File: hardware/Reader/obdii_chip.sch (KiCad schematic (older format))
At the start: 23 parts

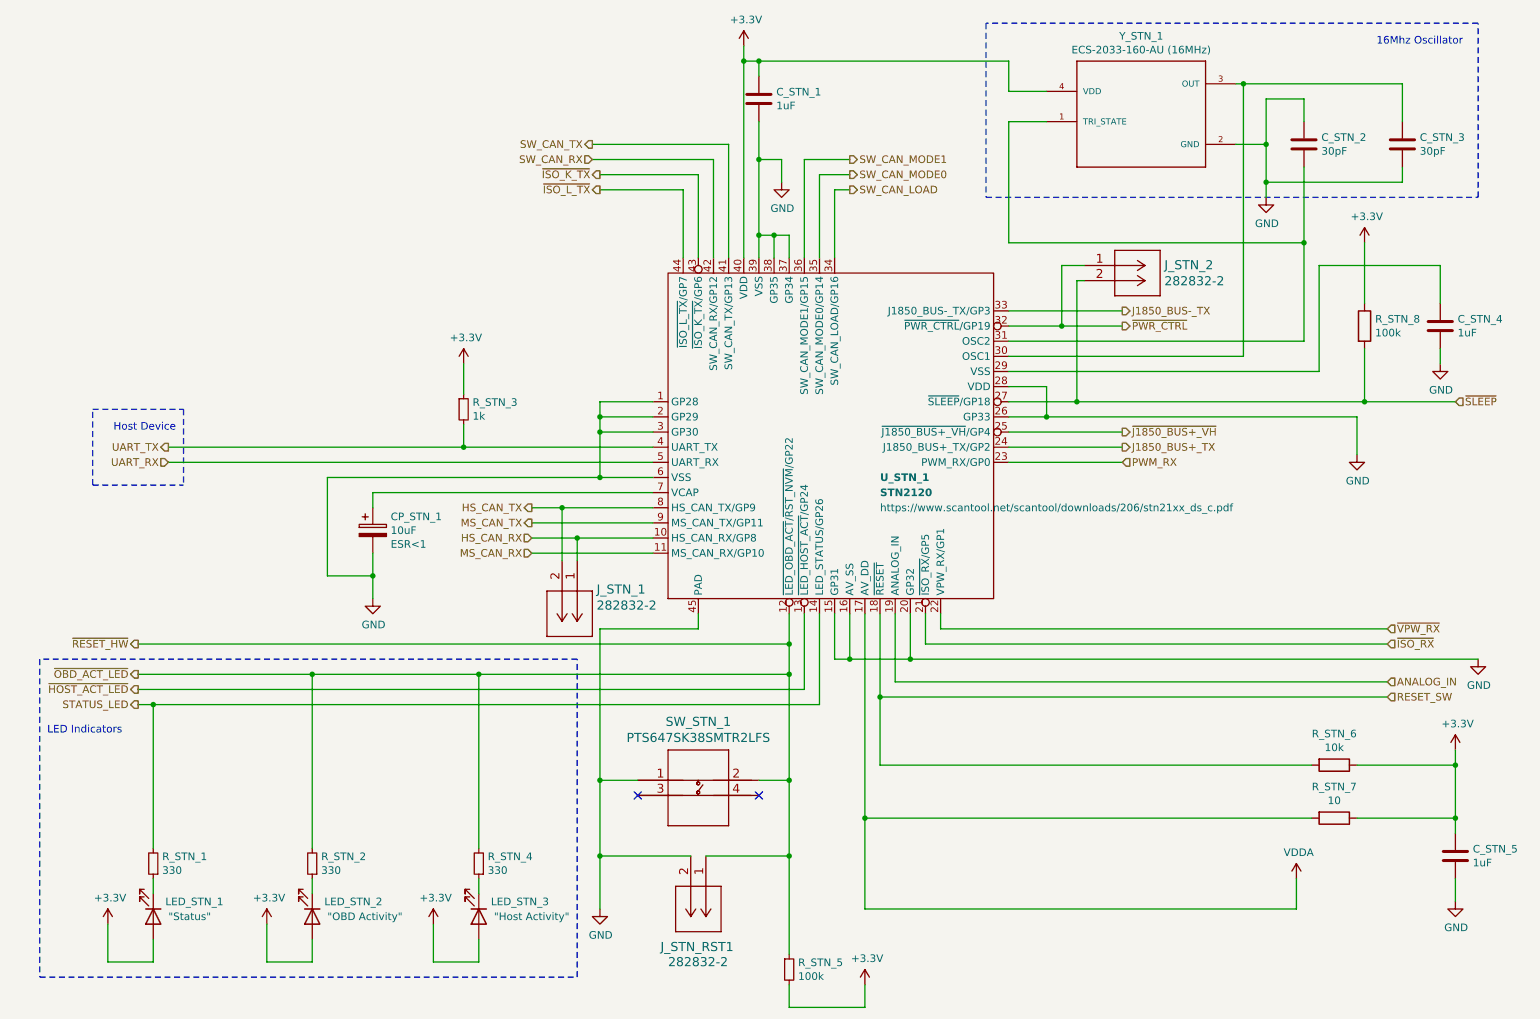
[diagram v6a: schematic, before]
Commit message: Fixed bugs in schematic. Updated BOM list. Swapped to using ESP32 holder. Updated PCB layout to v0.0.2. Updated schematic to v0.0.4
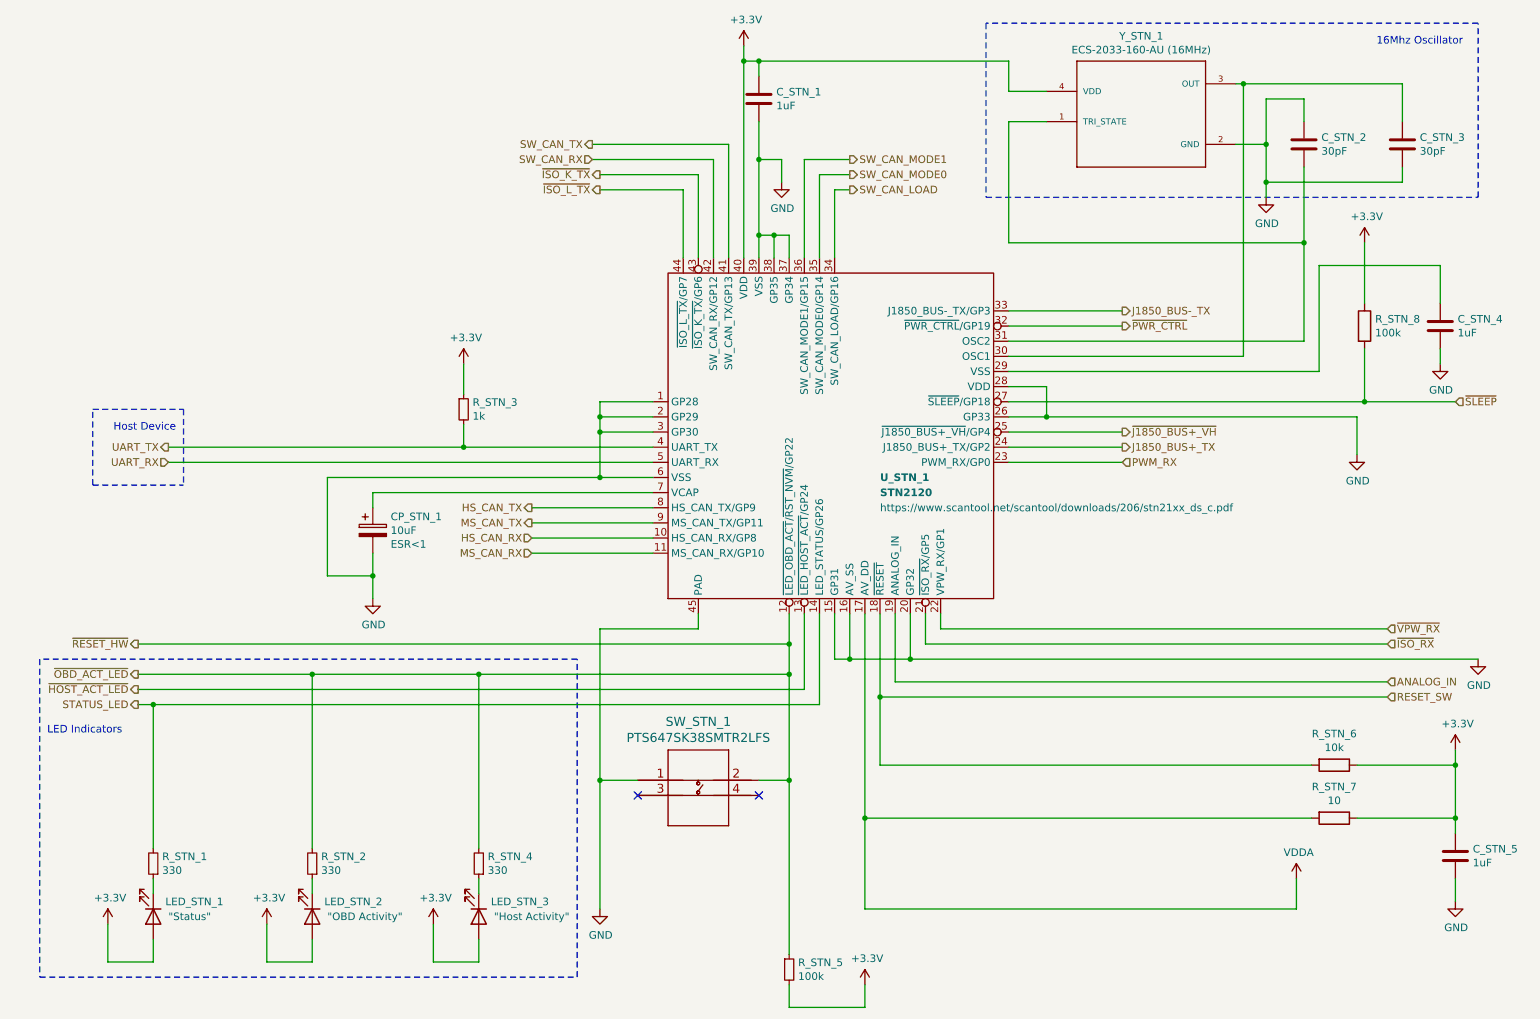
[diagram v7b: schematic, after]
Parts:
- removed J_STN_1, J_STN_2, J_STN_RST1: 282832-2, footprints:282832-2, symbol 2828322:282832-2
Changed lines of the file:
@@
 Sheet 10 19
 Title "CANnect Reader | OBDII Chip (STN2110)"
-Date "2020-10-27"
-Rev "0.0.03"
+Date "2020-10-28"
+Rev "0.0.04"
 Comp "CANtech"
 Comment1 "Created by Choong Jin Ng | jin8383@gmail.com"
@@
 	7100 1350 7100 2150
 Wire Wire Line
-	7100 3200 7550 3200
-Wire Wire Line
 	9450 2550 9450 2150
 Wire Wire Line
@@
 Wire Wire Line
 	9150 2300 9950 2300
-$Comp
-L 2828322:282832-2 J_STN_1
-U 1 1 5F9472A1
-P 4250 4250
-F 0 "J_STN_1" V 4439 4378 60  0000 L CNN
-F 1 "282832-2" V 4545 4378 60  0000 L CNN
-F 2 "footprints:282832-2" H 4650 4190 60  0001 C CNN
-F 3 "https://www.te.com/commerce/DocumentDelivery/DDEController?Action=srchrtrv&DocNm=282832&DocType=Customer+Drawing&DocLang=English" H 4250 4250 60  0001 C CNN
-F 4 "282832-2" H 4250 4250 50  0001 C CNN "Part Name"
-F 5 "DigiKey Canada" H 4250 4250 50  0001 C CNN "Vendor"
-F 6 "TE Connectivity AMP Connectors" H 4250 4250 50  0001 C CNN "Manufacturer"
-F 7 "A113314-ND" H 4250 4250 50  0001 C CNN "digikeypn"
-	1    4250 4250
-	0    1    1    0
-$EndComp
-Wire Wire Line
-	3950 3900 4150 3900
 Wire Wire Line
 	3950 4000 4750 4000
 Wire Wire Line
-	3950 4100 4250 4100
-Wire Wire Line
 	3950 4200 4750 4200
 Wire Wire Line
-	4150 4250 4150 3900
-Connection ~ 4150 3900
-Wire Wire Line
-	4150 3900 4750 3900
-Wire Wire Line
-	4250 4250 4250 4100
-Connection ~ 4250 4100
-Wire Wire Line
-	4250 4100 4750 4100
-$Comp
-L 2828322:282832-2 J_STN_2
-U 1 1 5F9BC402
-P 7600 2300
-F 0 "J_STN_2" H 8128 2303 60  0000 L CNN
-F 1 "282832-2" H 8128 2197 60  0000 L CNN
-F 2 "footprints:282832-2" H 8000 2240 60  0001 C CNN
-F 3 "https://www.te.com/commerce/DocumentDelivery/DDEController?Action=srchrtrv&DocNm=282832&DocType=Customer+Drawing&DocLang=English" H 7600 2300 60  0001 C CNN
-F 4 "282832-2" H 7600 2300 50  0001 C CNN "Part Name"
-F 5 "DigiKey Canada" H 7600 2300 50  0001 C CNN "Vendor"
-F 6 "TE Connectivity AMP Connectors" H 7600 2300 50  0001 C CNN "Manufacturer"
-F 7 "A113314-ND" H 7600 2300 50  0001 C CNN "digikeypn"
-	1    7600 2300
-	1    0    0    -1
-$EndComp
-Wire Wire Line
-	7100 2700 7450 2700
-Wire Wire Line
-	7600 2300 7450 2300
-Wire Wire Line
-	7450 2300 7450 2700
-Connection ~ 7450 2700
-Wire Wire Line
-	7450 2700 7850 2700
-Wire Wire Line
-	7600 2400 7550 2400
-Wire Wire Line
-	7550 2400 7550 3200
-Connection ~ 7550 3200
-Wire Wire Line
-	7550 3200 9450 3200
-Wire Wire Line
 	5650 7200 5650 7050
-$Comp
-L 2828322:282832-2 J_STN_RST1
-U 1 1 5FA37F1D
-P 5100 6200
-F 0 "J_STN_RST1" V 5700 5900 60  0000 L CNN
-F 1 "282832-2" V 5800 5950 60  0000 L CNN
-F 2 "footprints:282832-2" H 5500 6140 60  0001 C CNN
-F 3 "https://www.te.com/commerce/DocumentDelivery/DDEController?Action=srchrtrv&DocNm=282832&DocType=Customer+Drawing&DocLang=English" H 5100 6200 60  0001 C CNN
-F 4 "282832-2" H 5100 6200 50  0001 C CNN "Part Name"
-F 5 "DigiKey Canada" H 5100 6200 50  0001 C CNN "Vendor"
-F 6 "TE Connectivity AMP Connectors" H 5100 6200 50  0001 C CNN "Manufacturer"
-F 7 "A113314-ND" H 5100 6200 50  0001 C CNN "digikeypn"
-	1    5100 6200
-	0    1    1    0
-$EndComp
 Connection ~ 6250 5150
 Wire Wire Line
@@
 Connection ~ 5650 5700
 Wire Wire Line
-	5650 5700 5650 6200
-Wire Wire Line
 	4650 5700 4400 5700
 Connection ~ 4400 5700
 Wire Wire Line
-	4400 5700 4400 6200
-Wire Wire Line
 	5650 7200 6150 7200
 Wire Wire Line
 	6150 7200 6150 7050
-Wire Wire Line
-	5100 6200 5650 6200
-Connection ~ 5650 6200
-Wire Wire Line
-	5650 6200 5650 6850
-Wire Wire Line
-	5000 6200 4400 6200
-Connection ~ 4400 6200
-Wire Wire Line
-	4400 6200 4400 6550
 $Comp
 L PTS647SK38SMTR2LFS:PTS647SK38SMTR2LFS SW_STN_1
@@
 NoConn ~ 4650 5800
 NoConn ~ 5450 5800
+Wire Wire Line
+	3950 3900 4750 3900
+Wire Wire Line
+	3950 4100 4750 4100
+Wire Wire Line
+	7100 2700 7850 2700
+Wire Wire Line
+	7100 3200 9450 3200
+Wire Wire Line
+	5650 5700 5650 6850
+Wire Wire Line
+	4400 5700 4400 6550
 $EndSCHEMATC

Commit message: Revising reader
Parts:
- removed SW_STN_1: PTS647SK38SMTR2LFS, footprints:PTS647SK38SMTR2LFS, symbol PTS647SK38SMTR2LFS:PTS647SK38SMTR2LFS
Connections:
- net ~HOST_ACT_LED~: now also R_STN_4.2
- net ~OBD_ACT_LED~: no longer R_STN_4.2
- no-connect marks 2 -> 0
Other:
- note added: "Insert jumper here"
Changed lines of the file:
@@
 Sheet 10 19
 Title "CANnect Reader | OBDII Chip (STN2110)"
-Date "2020-10-28"
-Rev "0.0.04"
+Date "2020-11-19"
+Rev "0.0.05"
 Comp "CANtech"
 Comment1 "Created by Choong Jin Ng | jin8383@gmail.com"
@@
 U 1 1 5FC10F0A
 P 5650 6950
-F 0 "R_STN_5" H 5709 6996 50  0000 L CNN
-F 1 "100k" H 5709 6905 50  0000 L CNN
+F 0 "R_STN_5" H 5250 7000 50  0000 L CNN
+F 1 "100k" H 5350 6900 50  0000 L CNN
 F 2 "footprints:RESC1608X55N" H 5650 6950 50  0001 C CNN
 F 3 "https://www.yageo.com/upload/media/product/productsearch/datasheet/rchip/PYu-RT_1-to-0.01_RoHS_L_12.pdf" H 5650 6950 50  0001 C CNN
@@
 L power:+3.3V #PWR064
 U 1 1 5FC11757
-P 6150 7050
-F 0 "#PWR064" H 6150 6900 50  0001 C CNN
-F 1 "+3.3V" H 6165 7223 50  0000 C CNN
-F 2 "" H 6150 7050 50  0001 C CNN
-F 3 "" H 6150 7050 50  0001 C CNN
-	1    6150 7050
+P 5900 7050
+F 0 "#PWR064" H 5900 6900 50  0001 C CNN
+F 1 "+3.3V" H 5915 7223 50  0000 C CNN
+F 2 "" H 5900 7050 50  0001 C CNN
+F 3 "" H 5900 7050 50  0001 C CNN
+	1    5900 7050
 	1    0    0    -1
 $EndComp
@@
 	2500 5000 2500 6150
 Wire Wire Line
-	3600 5000 3600 6150
-Wire Wire Line
 	3600 6900 3300 6900
 Wire Wire Line
@@
 	1350 4800 5650 4800
 Wire Wire Line
-	1350 5100 5750 5100
+	1350 5100 3600 5100
 Wire Wire Line
 	1350 5200 1450 5200
@@
 Wire Wire Line
 	2500 5000 1350 5000
-Connection ~ 3600 5000
-Wire Wire Line
-	2500 5000 3600 5000
 Wire Wire Line
 	1450 5200 5850 5200
-Wire Wire Line
-	3600 5000 5650 5000
 Wire Notes Line
 	700  7000 4250 7000
@@
 	5050 4700 4400 4700
 Wire Wire Line
+	3950 3900 4750 3900
+Wire Wire Line
+	3950 4100 4750 4100
+Wire Wire Line
+	7100 2700 7850 2700
+Wire Wire Line
+	7100 3200 9450 3200
+Wire Wire Line
+	2500 5000 5650 5000
+Wire Wire Line
+	3600 6150 3600 5100
+Connection ~ 3600 5100
+Wire Wire Line
+	3600 5100 5750 5100
+Wire Wire Line
+	4400 5700 4400 6550
+Wire Wire Line
 	4400 4700 4400 5700
+Connection ~ 4400 5700
+Wire Wire Line
+	4650 5700 4400 5700
+Wire Wire Line
+	5650 5700 5650 6850
 Wire Wire Line
 	5650 5000 5650 5700
+Connection ~ 5650 5700
 Wire Wire Line
 	5450 5700 5650 5700
-Connection ~ 5650 5700
-Wire Wire Line
-	4650 5700 4400 5700
-Connection ~ 4400 5700
-Wire Wire Line
-	5650 7200 6150 7200
-Wire Wire Line
-	6150 7200 6150 7050
-$Comp
-L PTS647SK38SMTR2LFS:PTS647SK38SMTR2LFS SW_STN_1
-U 1 1 5F93A6E5
-P 4250 5700
-F 0 "SW_STN_1" H 5050 6087 60  0000 C CNN
-F 1 "PTS647SK38SMTR2LFS" H 5050 5981 60  0000 C CNN
-F 2 "footprints:PTS647SK38SMTR2LFS" H 5050 5940 60  0001 C CNN
-F 3 "https://www.ckswitches.com/media/2567/pts647.pdf" H 4250 5700 60  0001 C CNN
-F 4 "PTS647SK38SMTR2LFS" H 4250 5700 50  0001 C CNN "Part Name"
-F 5 "C&K" H 4250 5700 50  0001 C CNN "Manufacturer"
-F 6 "DigiKey Canada" H 4250 5700 50  0001 C CNN "Vendor"
-F 7 "PTS647SK38SMTR2LFSCT-ND" H 4250 5700 50  0001 C CNN "digikeypn"
-	1    4250 5700
-	1    0    0    -1
-$EndComp
-NoConn ~ 4650 5800
-NoConn ~ 5450 5800
-Wire Wire Line
-	3950 3900 4750 3900
-Wire Wire Line
-	3950 4100 4750 4100
-Wire Wire Line
-	7100 2700 7850 2700
-Wire Wire Line
-	7100 3200 9450 3200
-Wire Wire Line
-	5650 5700 5650 6850
-Wire Wire Line
-	4400 5700 4400 6550
+Wire Notes Line
+	4550 5450 4550 6000
+Wire Notes Line
+	4550 6000 5550 6000
+Wire Notes Line
+	5550 6000 5550 5450
+Wire Notes Line
+	5550 5450 4550 5450
+Text Notes 4700 5850 0    50   ~ 0
+Insert jumper here
+Wire Wire Line
+	5650 7200 5900 7200
+Wire Wire Line
+	5900 7200 5900 7050
 $EndSCHEMATC
